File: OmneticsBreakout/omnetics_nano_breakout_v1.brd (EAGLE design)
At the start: 26.1 x 15.2 mm, 2 parts

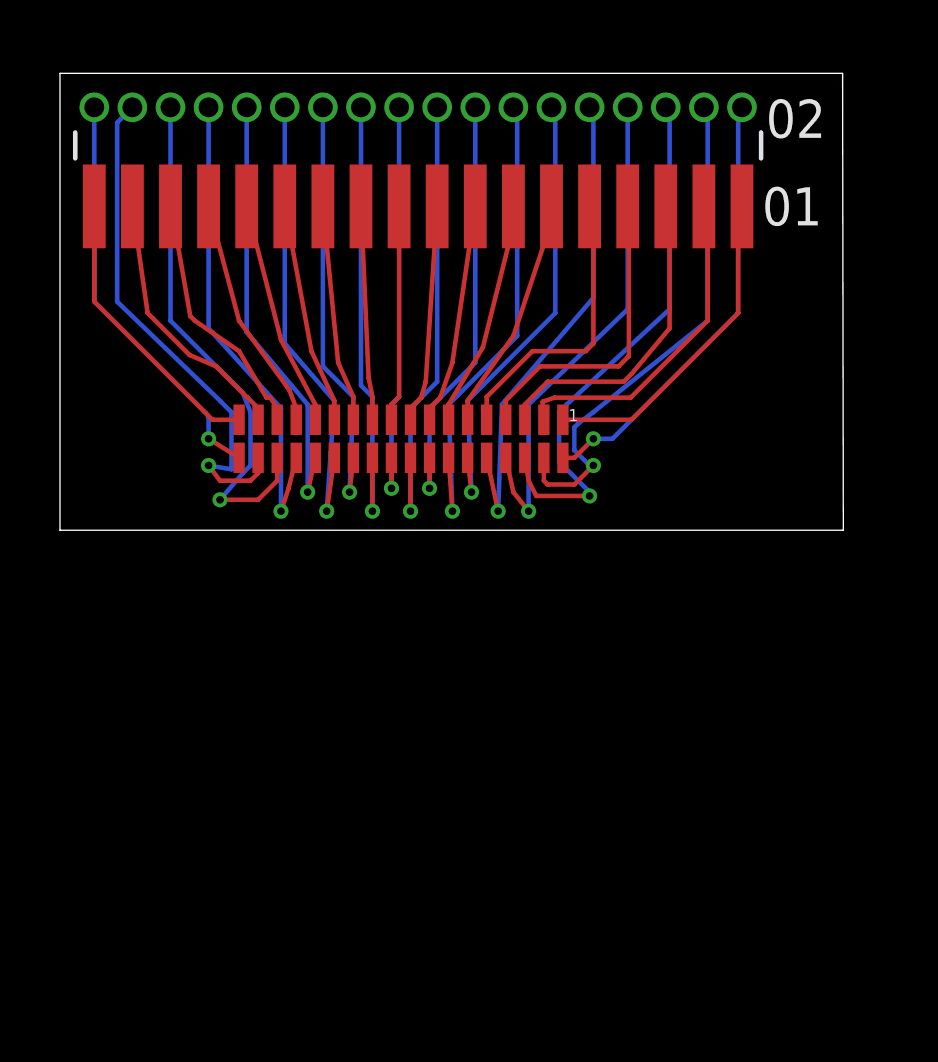
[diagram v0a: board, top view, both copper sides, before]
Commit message: updated pinouts of omnetics board
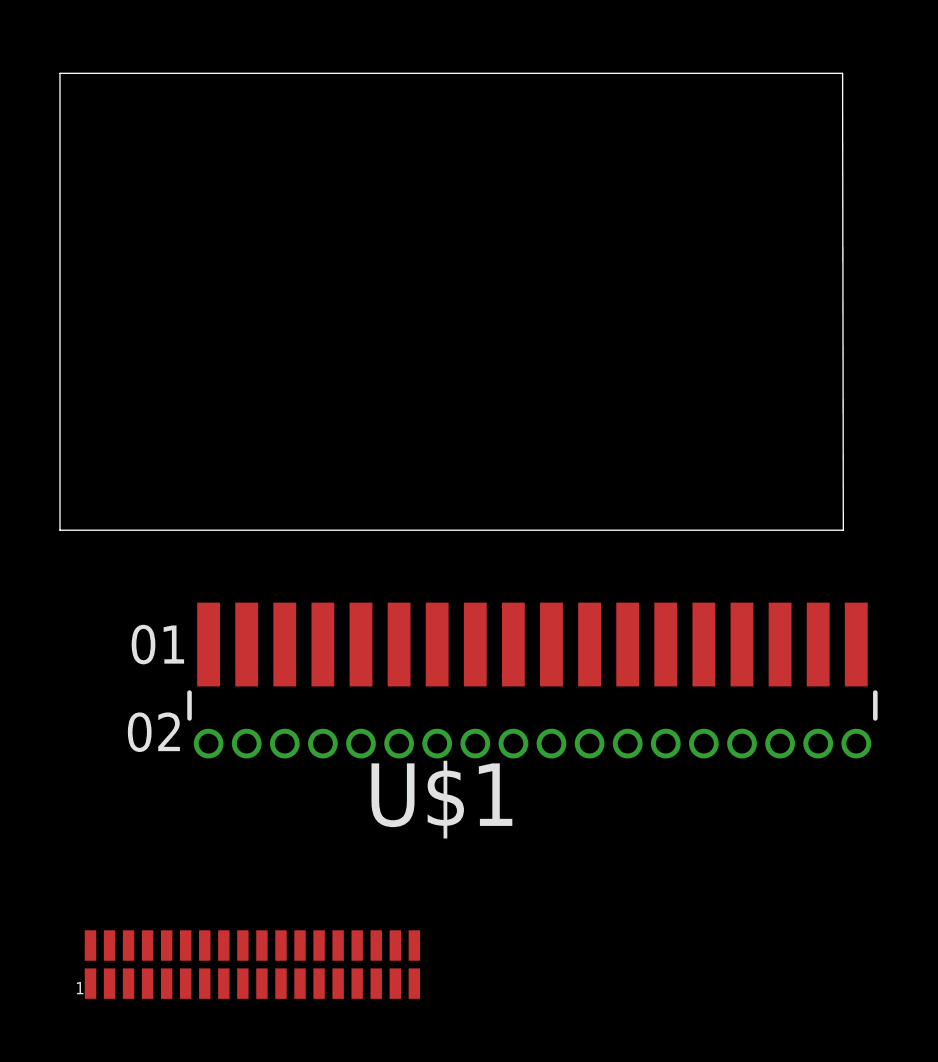
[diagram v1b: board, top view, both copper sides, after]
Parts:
- U$1: value OMNETICS_NANO_18X2 -> FTSH-118-01-L-MTINVERTED; device Sombeck_lib:OMNETICS_NANO_18X2 -> tuckerLib:FTSH-118-01-L-MT-INVERTED
- U$2: value FTSH-118-01-L-MTINVERTED -> OMNETICS_NANO_18X2; device tuckerLib:FTSH-118-01-L-MT-INVERTED -> Sombeck_lib:OMNETICS_NANO_18X2
- moved U$2 28.8 mm to (1.02, -15.1), turned to 0 degrees
- moved U$1 8.32 mm to (15.7, -4.57), turned to 0 degrees
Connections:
- removed net N$19: U$1.P36, U$2.2
- removed net N$20: U$1.P35, U$2.4
- removed net N$21: U$1.P34, U$2.6
- removed net N$22: U$1.P33, U$2.8
- removed net N$23: U$1.P32, U$2.10
- removed net N$24: U$1.P31, U$2.12
- removed net N$25: U$1.P30, U$2.14
- removed net N$26: U$1.P29, U$2.16
- removed net N$27: U$1.P28, U$2.18
- removed net N$28: U$1.P19, U$2.36
- removed net N$29: U$1.P20, U$2.34
- removed net N$30: U$1.P21, U$2.32
- removed net N$31: U$1.P22, U$2.30
- removed net N$32: U$1.P23, U$2.28
- removed net N$33: U$1.P24, U$2.26
- removed net N$34: U$1.P25, U$2.24
- removed net N$35: U$1.P26, U$2.22
- removed net N$36: U$1.P27, U$2.20
- new net AGND: U$1.33, U$2.REF33
- new net GND: U$1.34, U$1.35, U$2.GND0, U$2.GND34
- net N$1: now also U$1.1, U$2.P_1; no longer U$1.P1, U$2.1
- net N$10: now also U$1.18, U$2.P_18; no longer U$1.P10, U$2.19
- net N$11: now also U$1.20, U$2.P_20; no longer U$1.P11, U$2.21
- net N$12: now also U$1.22, U$2.P_22; no longer U$1.P12, U$2.23
- net N$13: now also U$1.24, U$2.P_24; no longer U$1.P13, U$2.25
- net N$14: now also U$1.26, U$2.P_26; no longer U$1.P14, U$2.27
- net N$15: now also U$1.28, U$2.P_28; no longer U$1.P15, U$2.29
- net N$16: now also U$1.30, U$2.P_30; no longer U$1.P16, U$2.31
- net N$17: now also U$1.32, U$2.P_32; no longer U$1.P17, U$2.33
- net N$18: now also U$1.3, U$2.P_3; no longer U$1.P18, U$2.35
- net N$2: now also U$1.2, U$2.P_2; no longer U$1.P2, U$2.3
- net N$3: now also U$1.4, U$2.P_4; no longer U$1.P3, U$2.5
- net N$4: now also U$1.6, U$2.P_6; no longer U$1.P4, U$2.7
- net N$5: now also U$1.8, U$2.P_8; no longer U$1.P5, U$2.9
- net N$6: now also U$1.10, U$2.P_10; no longer U$1.P6, U$2.11
- net N$7: now also U$1.12, U$2.P_12; no longer U$1.P7, U$2.13
- net N$8: now also U$1.14, U$2.P_14; no longer U$1.P8, U$2.15
- net N$9: now also U$1.16, U$2.P_16; no longer U$1.P9, U$2.17
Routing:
- net N$21: track 18.1 -> 0.00 mm, vias 1 -> 0
- net N$30: track 17.4 -> 0.00 mm, vias 1 -> 0
- net N$20: track 17.2 -> 0.00 mm, vias 1 -> 0
- net N$29: track 17.2 -> 0.00 mm, vias 1 -> 0
- net N$22: track 16.9 -> 0.00 mm, vias 1 -> 0
- net N$23: track 16.5 -> 0.00 mm, vias 1 -> 0
- net N$25: track 16.2 -> 0.00 mm, vias 1 -> 0
- net N$31: track 16.2 -> 0.00 mm, vias 1 -> 0
- net N$33: track 15.9 -> 0.00 mm, vias 1 -> 0
- net N$27: track 15.6 -> 0.00 mm, vias 1 -> 0
- net N$35: track 15.4 -> 0.00 mm, vias 1 -> 0
- net N$24: track 15.2 -> 0.00 mm, vias 1 -> 0
- net N$19: track 14.8 -> 0.00 mm, vias 1 -> 0
- net N$32: track 14.7 -> 0.00 mm, vias 1 -> 0
- net N$34: track 14.4 -> 0.00 mm, vias 1 -> 0
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
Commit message: omnetics breakout board update
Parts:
- removed U$1: FTSH-118-01-L-MTINVERTED, tuckerLib:FTSH-118-01-L-MT-INVERTED
- added U$3: FTSH-118-01-L-MTREGULAR, tuckerLib:FTSH-118-01-L-MT
- moved U$2 18.5 mm to (7.37, 2.22)
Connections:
- new net N$19: U$2.P_5, U$3.5
- new net N$20: U$2.P_7, U$3.7
- new net N$21: U$2.P_9, U$3.9
- new net N$22: U$2.P_11, U$3.11
- new net N$23: U$2.P_13, U$3.13
- new net N$24: U$2.P_15, U$3.15
- new net N$25: U$2.P_17, U$3.17
- new net N$26: U$2.P_19, U$3.19
- new net N$27: U$2.P_21, U$3.21
- new net N$28: U$2.P_23, U$3.23
- new net N$29: U$2.P_25, U$3.25
- new net N$30: U$2.P_27, U$3.27
- new net N$31: U$2.P_29, U$3.29
- new net N$32: U$2.P_31, U$3.31
- net AGND: now also U$3.33; no longer U$1.33
- net GND: now also U$3.34, U$3.35; no longer U$1.34, U$1.35
- net N$1: now also U$3.1; no longer U$1.1
- net N$10: now also U$3.18; no longer U$1.18
- net N$11: now also U$3.20; no longer U$1.20
- net N$12: now also U$3.22; no longer U$1.22
- net N$13: now also U$3.24; no longer U$1.24
- net N$14: now also U$3.26; no longer U$1.26
- net N$15: now also U$3.28; no longer U$1.28
- net N$16: now also U$3.30; no longer U$1.30
- net N$17: now also U$3.32; no longer U$1.32
- net N$18: now also U$3.3; no longer U$1.3
- net N$2: now also U$3.2; no longer U$1.2
- net N$3: now also U$3.4; no longer U$1.4
- net N$4: now also U$3.6; no longer U$1.6
- net N$5: now also U$3.8; no longer U$1.8
- net N$6: now also U$3.10; no longer U$1.10
- net N$7: now also U$3.12; no longer U$1.12
- net N$8: now also U$3.14; no longer U$1.14
- net N$9: now also U$3.16; no longer U$1.16
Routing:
- net GND: track 0.00 -> 34.2 mm, vias 0 -> 2
- net N$10: track 0.00 -> 27.0 mm, vias 0 -> 1
- net N$12: track 0.00 -> 26.9 mm, vias 0 -> 1
- net N$11: track 0.00 -> 26.5 mm, vias 0 -> 1
- net N$8: track 0.00 -> 25.9 mm, vias 0 -> 1
- net N$9: track 0.00 -> 25.3 mm, vias 0 -> 1
- net N$14: track 0.00 -> 25.3 mm, vias 0 -> 1
- net N$13: track 0.00 -> 24.8 mm, vias 0 -> 1
- net N$6: track 0.00 -> 24.5 mm, vias 0 -> 1
- net N$7: track 0.00 -> 23.9 mm, vias 0 -> 1
- net N$16: track 0.00 -> 23.6 mm, vias 0 -> 1
- net N$15: track 0.00 -> 23.2 mm, vias 0 -> 1
- net N$4: track 0.00 -> 23.1 mm, vias 0 -> 1
- net N$5: track 0.00 -> 22.5 mm, vias 0 -> 1
- net N$3: track 0.00 -> 21.6 mm, vias 0 -> 1
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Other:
- board size 26.1 x 15.2 mm -> 26.2 x 15.8 mm
